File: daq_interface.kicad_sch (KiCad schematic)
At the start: 18 parts, among them J5 DAQ_IO

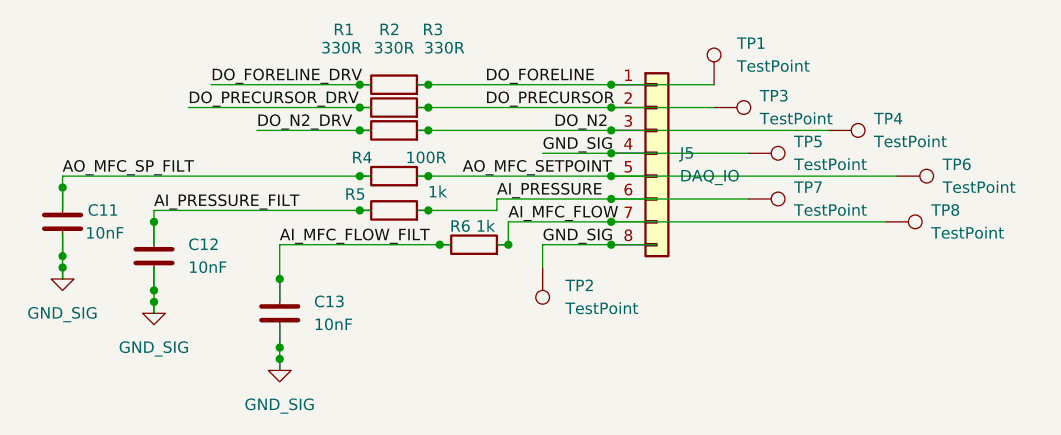
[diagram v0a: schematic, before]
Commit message: Clean up duplicates in schematic components
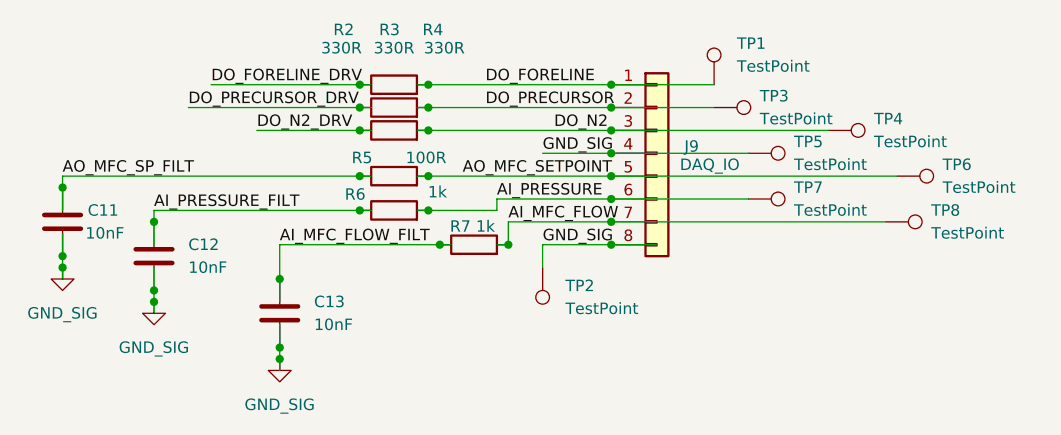
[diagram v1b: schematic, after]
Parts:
- renumbered J5 to J9, R1 to R2, R2 to R3, R3 to R4, R4 to R5, R5 to R6, R6 to R7
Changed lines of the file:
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@@
 		(on_board yes)
 		(dnp no)
-		(property "Reference" "R6"
+		(property "Reference" "R7"
 			(at 143.256 93.218 90)
 			(effects
@@
 			(project "ald_control_board"
 				(path "/0db39e9c-e7a7-46b4-b6c2-b1f3e7389c4f/a79275c5-8d52-4258-805e-88046f0b4eaf"
-					(reference "R6")
+					(reference "R7")
 					(unit 1)
 				)
@@
 		(on_board yes)
 		(dnp no)
-		(property "Reference" "R2"
+		(property "Reference" "R3"
 			(at 135.382 71.374 90)
 			(effects
@@
 			(project ""
 				(path "/0db39e9c-e7a7-46b4-b6c2-b1f3e7389c4f/a79275c5-8d52-4258-805e-88046f0b4eaf"
-					(reference "R2")
+					(reference "R3")
 					(unit 1)
 				)
@@
 		(on_board yes)
 		(dnp no)
-		(property "Reference" "R3"
+		(property "Reference" "R4"
 			(at 140.208 71.374 90)
 			(effects
@@
 			(project ""
 				(path "/0db39e9c-e7a7-46b4-b6c2-b1f3e7389c4f/a79275c5-8d52-4258-805e-88046f0b4eaf"
-					(reference "R3")
+					(reference "R4")
 					(unit 1)
 				)
@@
 		(on_board yes)
 		(dnp no)
-		(fields_autoplaced yes)
-		(property "Reference" "J5"
-			(at 167.64 85.0899 0)
+		(property "Reference" "J9"
+			(at 168.148 84.328 0)
 			(effects
 				(font
@@
 		)
 		(property "Value" "DAQ_IO"
-			(at 167.64 87.6299 0)
+			(at 167.64 86.3599 0)
 			(effects
 				(font
@@
 			(project ""
 				(path "/0db39e9c-e7a7-46b4-b6c2-b1f3e7389c4f/a79275c5-8d52-4258-805e-88046f0b4eaf"
-					(reference "J5")
+					(reference "J9")
 					(unit 1)
 				)
@@
 		(on_board yes)
 		(dnp no)
-		(property "Reference" "R4"
+		(property "Reference" "R5"
 			(at 132.334 85.598 90)
 			(effects
@@
 			(project ""
 				(path "/0db39e9c-e7a7-46b4-b6c2-b1f3e7389c4f/a79275c5-8d52-4258-805e-88046f0b4eaf"
-					(reference "R4")
+					(reference "R5")
 					(unit 1)
 				)
@@
 		(on_board yes)
 		(dnp no)
-		(property "Reference" "R1"
+		(property "Reference" "R2"
 			(at 130.302 71.374 90)
 			(effects
@@
 			(project ""
 				(path "/0db39e9c-e7a7-46b4-b6c2-b1f3e7389c4f/a79275c5-8d52-4258-805e-88046f0b4eaf"
-					(reference "R1")
+					(reference "R2")
 					(unit 1)
 				)
@@
 		(on_board yes)
 		(dnp no)
-		(property "Reference" "R5"
+		(property "Reference" "R6"
 			(at 131.572 89.662 90)
 			(effects
@@
 			(project "ald_control_board"
 				(path "/0db39e9c-e7a7-46b4-b6c2-b1f3e7389c4f/a79275c5-8d52-4258-805e-88046f0b4eaf"
-					(reference "R5")
-					(unit 1)
-				)
+					(reference "R6")
+					(unit 1)
+				)

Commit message: Clean up duplicates in schematic components and assign footprints
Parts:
- C11, C12, C13: footprint (none) -> Capacitor_SMD:C_0805_2012Metric_Pad1.18x1.45mm_HandSolder
- J9: footprint (none) -> Connector_PinHeader_2.54mm:PinHeader_1x08_P2.54mm_Vertical
- R2, R3, R4, R5, R6, R7: footprint (none) -> Resistor_SMD:R_0805_2012Metric_Pad1.20x1.40mm_HandSolder
- TP1, TP2, TP3, TP4, TP5, TP6, TP7, TP8: footprint (none) -> TestPoint:TestPoint_Loop_D2.50mm_Drill1.0mm
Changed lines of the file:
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@@
 			)
 		)
-		(property "Footprint" ""
+		(property "Footprint" "Resistor_SMD:R_0805_2012Metric_Pad1.20x1.40mm_HandSolder"
 			(at 144.78 97.028 90)
 			(effects
@@
 			)
 		)
-		(property "Footprint" ""
+		(property "Footprint" "TestPoint:TestPoint_Loop_D2.50mm_Drill1.0mm"
 			(at 175.26 90.17 0)
 			(effects
@@
 			)
 		)
-		(property "Footprint" ""
+		(property "Footprint" "Resistor_SMD:R_0805_2012Metric_Pad1.20x1.40mm_HandSolder"
 			(at 135.89 81.788 90)
 			(effects
@@
 			)
 		)
-		(property "Footprint" ""
+		(property "Footprint" "TestPoint:TestPoint_Loop_D2.50mm_Drill1.0mm"
 			(at 184.15 87.63 0)
 			(effects
@@
 			)
 		)
-		(property "Footprint" ""
+		(property "Footprint" "Capacitor_SMD:C_0805_2012Metric_Pad1.18x1.45mm_HandSolder"
 			(at 110.1852 100.33 0)
 			(effects
@@
 			)
 		)
-		(property "Footprint" ""
+		(property "Footprint" "TestPoint:TestPoint_Loop_D2.50mm_Drill1.0mm"
 			(at 191.77 92.71 0)
 			(effects
@@
 			)
 		)
-		(property "Footprint" ""
+		(property "Footprint" "TestPoint:TestPoint_Loop_D2.50mm_Drill1.0mm"
 			(at 190.5 97.79 0)
 			(effects
@@
 			)
 		)
-		(property "Footprint" ""
+		(property "Footprint" "Resistor_SMD:R_0805_2012Metric_Pad1.20x1.40mm_HandSolder"
 			(at 135.89 84.328 90)
 			(effects
@@
 			)
 		)
-		(property "Footprint" ""
+		(property "Footprint" "TestPoint:TestPoint_Loop_D2.50mm_Drill1.0mm"
 			(at 171.45 85.09 0)
 			(effects
@@
 			)
 		)
-		(property "Footprint" ""
+		(property "Footprint" "Connector_PinHeader_2.54mm:PinHeader_1x08_P2.54mm_Vertical"
 			(at 165.1 85.09 0)
 			(effects
@@
 			)
 		)
-		(property "Footprint" ""
+		(property "Footprint" "Capacitor_SMD:C_0805_2012Metric_Pad1.18x1.45mm_HandSolder"
 			(at 100.0252 96.52 0)
 			(effects
@@
 			)
 		)
-		(property "Footprint" ""
+		(property "Footprint" "Resistor_SMD:R_0805_2012Metric_Pad1.20x1.40mm_HandSolder"
 			(at 135.89 89.408 90)
 			(effects
@@
 			)
 		)
-		(property "Footprint" ""
+		(property "Footprint" "TestPoint:TestPoint_Loop_D2.50mm_Drill1.0mm"
 			(at 176.53 77.47 0)
 			(effects
@@
 			)
 		)
-		(property "Footprint" ""
+		(property "Footprint" "Capacitor_SMD:C_0805_2012Metric_Pad1.18x1.45mm_HandSolder"
 			(at 124.1552 106.68 0)
 			(effects
@@
 			)
 		)
-		(property "Footprint" ""
+		(property "Footprint" "Resistor_SMD:R_0805_2012Metric_Pad1.20x1.40mm_HandSolder"
 			(at 135.89 79.248 90)
 			(effects
@@
 			)
 		)
-		(property "Footprint" ""
+		(property "Footprint" "Resistor_SMD:R_0805_2012Metric_Pad1.20x1.40mm_HandSolder"
 			(at 135.89 93.218 90)
 			(effects
@@
 			)
 		)
-		(property "Footprint" ""
+		(property "Footprint" "TestPoint:TestPoint_Loop_D2.50mm_Drill1.0mm"
 			(at 175.26 95.25 0)
 			(effects
@@
 			)
 		)
-		(property "Footprint" ""
+		(property "Footprint" "TestPoint:TestPoint_Loop_D2.50mm_Drill1.0mm"
 			(at 147.32 97.79 0)
 			(effects
